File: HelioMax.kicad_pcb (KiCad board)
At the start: 2 copper layers, 185.3 x 159 mm, 75 parts, among them J2 Conn_01x07, J3 Conn_01x07, J4 Conn_01x07, J5 Conn_01x07, J8 Conn_01x07, J9 Conn_01x07, SW0:10 SW0:3, SW0:11 SW0:2, SW0:12 SW0:1, SW0:7 SW0:6, SW0:8 SW0:5, SW0:9 SW0:4, SW1:10 SW1:3, SW1:11 SW1:2, SW1:12 SW1:1, SW1:13 SW1:0, SW1:9 SW1:4, SW2:10 SW2:3, SW2:11 SW2:2, SW2:12 SW2:1, SW2:13 SW2:0, SW2:7 SW2:6, SW2:8 SW2:5, SW2:9 SW2:4, SW3:10 SW3:3, SW3:11 SW3:2, SW3:12 SW3:1, SW3:13 SW3:0, SW3:8 SW3:5, SW3:9 SW3:4, SW4:10 SW4:3, SW4:11 SW4:2, SW4:12 SW4:1, SW4:13 SW4:0, SW4:7 SW4:6, SW4:8 SW4:5, SW4:9 SW4:4, SW5:10 SW5:3, SW5:11 SW5:2, SW5:12 SW5:1, SW5:13 SW5:0, SW5:7 SW5:6, SW5:8 SW5:5, SW5:9 SW5:4, SW6:10 SW6:3, SW6:11 SW6:2, SW6:12 SW6:1, SW6:13 SW6:0, SW6:7 SW6:6, SW6:8 SW6:5, SW6:9 SW6:4

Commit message: Fixed edge cuts. Lots of DRC errors.
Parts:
- added ?: , , F.Cu at (85.2, 53.6)
- added ?: , , F.Cu at (40.5, 53.6)
- added ?: , , F.Cu at (40.5, 21.7)
- added A1: RaspberryPi_Pico, Module_RaspberryPi_Pico:RaspberryPi_Pico_Original_SMD_MountingHoles_HandSolder_Castellated, F.Cu at (63.1, 37.9)
- added J1: Conn_01x01_Pin, Connector_PinHeader_1.00mm:PinHeader_1x01_P1.00mm_Vertical, F.Cu at (48.1, 24.6)
- added J10: Conn_01x07, Connector_JST:JST_SH_SM08B-SRSS-TB_1x08-1MP_P1.00mm_Horizontal, F.Cu at (80.0, 20.9)
- added J11: Conn_01x07, Connector_JST:JST_SH_SM08B-SRSS-TB_1x08-1MP_P1.00mm_Horizontal, F.Cu at (64.5, 20.9)
- added J6: Conn_01x07, Connector_JST:JST_SH_SM08B-SRSS-TB_1x08-1MP_P1.00mm_Horizontal, F.Cu at (50.4, 54.7)
- added J7: Conn_01x07, Connector_JST:JST_SH_SM08B-SRSS-TB_1x08-1MP_P1.00mm_Horizontal, F.Cu at (71.6, 54.7)
- moved ? 70.4 mm to (209.5, 39.8)
- moved H99 70.4 mm to (121.1, 182.4)
- moved J3 70.4 mm to (150.5, 151.7)
- moved S1 70.4 mm to (119.7, 160.3)
- moved S2 70.4 mm to (138.8, 160.3)
- moved STITCHING_VIA 70.4 mm to (209.0, 74.1)
- moved STITCHING_VIA 70.4 mm to (152.4, 64.4)
- moved STITCHING_VIA 70.4 mm to (153.6, 77.0)
- moved STITCHING_VIA 70.4 mm to (190.6, 75.2)
- moved STITCHING_VIA 70.4 mm to (170.8, 134.0)
- moved STITCHING_VIA 70.4 mm to (94.5, 153.6)
- moved STITCHING_VIA 70.4 mm to (190.2, 138.6)
- moved STITCHING_VIA 70.4 mm to (208.9, 138.7)
- moved STITCHING_VIA 70.4 mm to (228.1, 137.1)
- moved SW0:10 70.4 mm to (138.8, 160.3)
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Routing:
- net Net-(A1-LED_OUT): track 0.00 -> 63.4 mm
- net Net-(A1-~{SMPS_PS}): track 0.00 -> 57.0 mm
- net Net-(A1-GPIO14): track 0.00 -> 38.4 mm
- net Net-(A1-GPIO15): track 0.00 -> 29.3 mm
- net Net-(J1-Pin_1): track 0.00 -> 20.3 mm
- net Net-(A1-GPIO0): track 0.00 -> 12.3 mm
- net Net-(A1-GPIO16): track 0.00 -> 11.9 mm
- net Net-(A1-GPIO1): track 0.00 -> 10.9 mm
- net Net-(A1-GPIO7): track 0.00 -> 10.9 mm
- net Net-(A1-GPIO6): track 0.00 -> 10.2 mm
- net Net-(A1-GPIO17): track 0.00 -> 10.1 mm
- net Net-(A1-GPIO8): track 0.00 -> 9.11 mm
- net Net-(A1-GPIO21): track 0.00 -> 9.11 mm
- net Net-(A1-GPIO13): track 0.00 -> 8.82 mm
- net Net-(A1-GPIO9): track 0.00 -> 7.90 mm
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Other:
- board size 185.3 x 159 mm -> 240.8 x 162.9 mm
- board text added: "Raspberry Pi Pico TP4 and TP5 must be modded to expose GP23 and GP25 respectively. J1 to be connected externally to GP24."
- board text added: "TP4"
- board text added: "TP5"

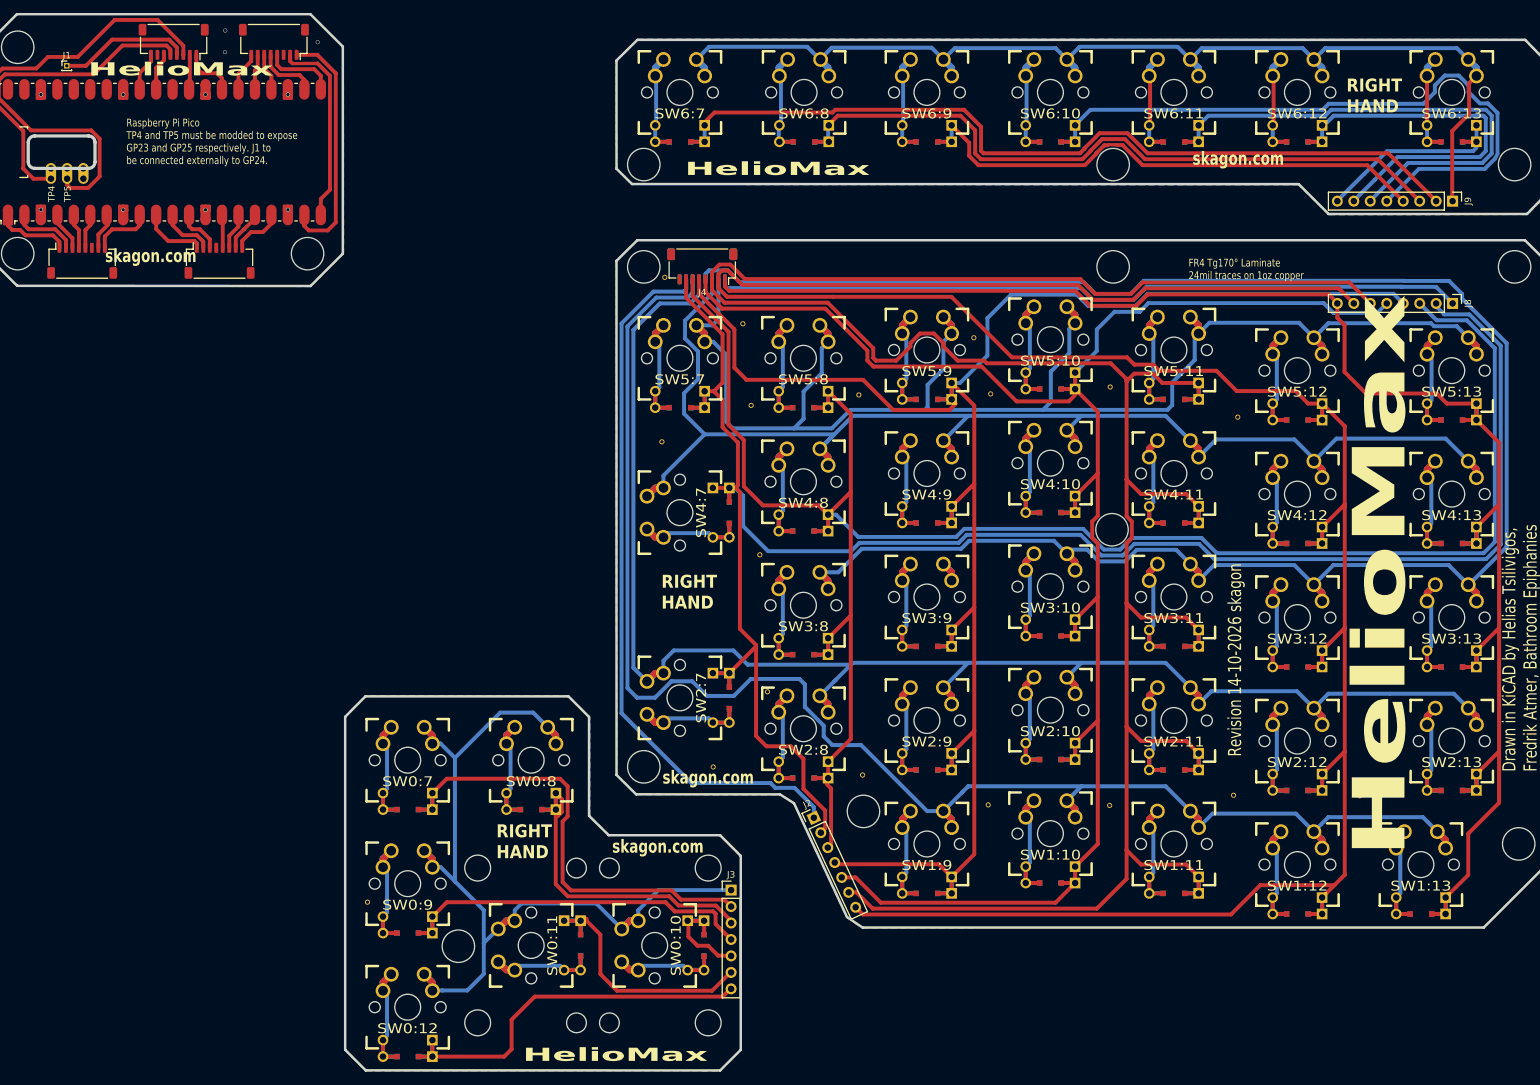
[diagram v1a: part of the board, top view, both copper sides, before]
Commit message: Updated switch footprint and fixed all wiring.
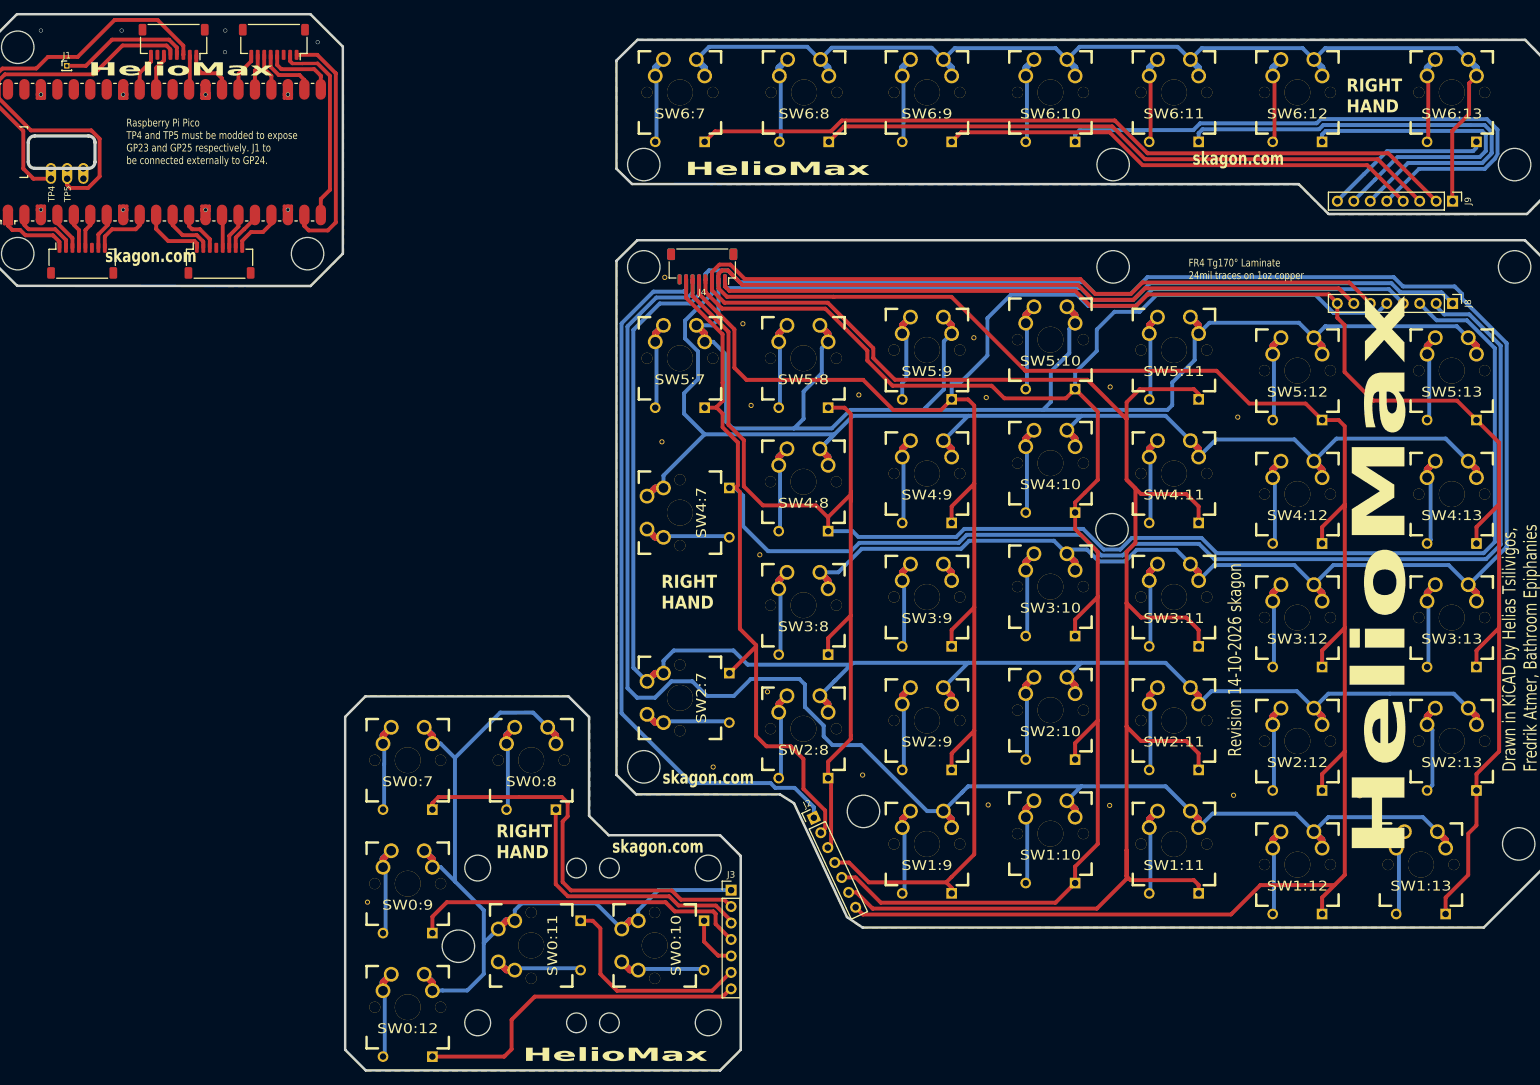
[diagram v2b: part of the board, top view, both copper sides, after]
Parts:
- SW0:10, SW0:11, SW0:12, SW0:7, SW0:8, SW0:9, SW1:10, SW1:11, SW1:12, SW1:13, SW1:9, SW2:10, SW2:11, SW2:12, SW2:13, SW2:7, SW2:8, SW2:9, SW3:10, SW3:11, SW3:12, SW3:13, SW3:8, SW3:9, SW4:10, SW4:11, SW4:12, SW4:13, SW4:7, SW4:8, SW4:9, SW5:10, SW5:11, SW5:12, SW5:13, SW5:7, SW5:8, SW5:9, SW6:10, SW6:11, SW6:12, SW6:13, SW6:7, SW6:8, SW6:9: footprint ErgoDOX pcb:MX_FLIP_DIODE -> ErgoDOX pcb:MX_FLIP_CLEAN
- moved STITCHING_VIA 0.89 mm to (189.9, 75.8)
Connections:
- J10 pad MP: GND -> (no net)
- J11 pad MP: GND -> (no net)
- J6 pad MP: GND -> (no net)
- J7 pad MP: GND -> (no net)
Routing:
- net /COL3: track 393.8 -> 361.6 mm
- net /COL6: track 491.5 -> 461.9 mm
- net /COL5: track 455.4 -> 429.4 mm
- net /COL1: track 514.9 -> 490.3 mm
- net /COL2: track 507.9 -> 483.3 mm
- net /COL0: track 275.2 -> 251.9 mm
- net /COL4: track 407.6 -> 386.4 mm
- net Net-(SW2:7-A): track 19.4 -> 16.4 mm
- net Net-(SW4:7-A): track 19.4 -> 16.4 mm
- net Net-(SW0:10-A): track 19.4 -> 16.4 mm
- net Net-(SW2:12-A): track 19.4 -> 16.4 mm
- net Net-(SW5:7-A): track 19.4 -> 16.4 mm
- net Net-(SW5:12-A): track 19.4 -> 16.4 mm
- net Net-(SW3:12-A): track 19.4 -> 16.4 mm
- net Net-(SW1:12-A): track 19.4 -> 16.4 mm
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
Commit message: Fixed most DRC problems, new vias, modified switch footprints.
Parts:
- removed STITCHING_VIA (x18): ~, lib_footprints:STITCHING_VIA
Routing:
- net /ROW3: track 317.5 -> 320.8 mm
- net /COL2: track 483.3 -> 486.3 mm
- net /COL5: track 429.4 -> 428.1 mm
- net /ROW1: track 249.8 -> 248.7 mm
- net /COL3: track 361.6 -> 362.6 mm
- net /ROW2: track 260.8 -> 260.0 mm
- net GND: vias 13 -> 47

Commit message: Replace relic holes, include fonts, general clean-up and rewiring.
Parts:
- removed ? (x6): , 
- removed H99: MECHANICAL, ErgoDOXmech
- added H1: MountingHole, MountingHole:MountingHole_3.2mm_M3, F.Cu at (134.6, 60.2)
- added H10: MountingHole, MountingHole:MountingHole_3.2mm_M3, F.Cu at (206.2, 44.2)
- added H11: MountingHole, MountingHole:MountingHole_3.2mm_M3, F.Cu at (268.1, 44.2)
- added H12: MountingHole, MountingHole:MountingHole_3.2mm_M3, F.Cu at (29.6, 29.2)
- added H13: MountingHole, MountingHole:MountingHole_3.2mm_M3, F.Cu at (29.6, 61.0)
- added H14: MountingHole, MountingHole:MountingHole_3.2mm_M3, F.Cu at (74.3, 61.0)
- added H2: MountingHole, MountingHole:MountingHole_3.2mm_M3, F.Cu at (207.0, 60.2)
- added H3: MountingHole, MountingHole:MountingHole_3.2mm_M3, F.Cu at (269.0, 60.2)
- added H4: MountingHole, MountingHole:MountingHole_3.2mm_M3, F.Cu at (134.6, 137.3)
- added H5: MountingHole, MountingHole:MountingHole_3.2mm_M3, F.Cu at (206.9, 100.7)
- added H6: MountingHole, MountingHole:MountingHole_3.2mm_M3, F.Cu at (269.6, 149.2)
- added H7: MountingHole, MountingHole:MountingHole_3.2mm_M3, F.Cu at (168.9, 150.0)
- added H8: MountingHole, MountingHole:MountingHole_3.2mm_M3, F.Cu at (100.9, 167.8)
- added H9: MountingHole, MountingHole:MountingHole_3.2mm_M3, F.Cu at (133.8, 44.2)
- moved A1 13.3 mm to (52.2, 45.4)
- moved J6 13.3 mm to (39.5, 62.1)
- moved J7 13.3 mm to (60.7, 62.1)
- moved J10 13.3 mm to (69.1, 28.4)
- moved J11 13.3 mm to (53.6, 28.4)
- moved J3 10.6 mm to (143.0, 159.1)
- moved S2 10.6 mm to (131.2, 167.7)
- moved SW0:10 10.6 mm to (131.2, 167.7)
- moved SW0:12 10.6 mm to (93.1, 177.2)
- moved SW0:7 10.6 mm to (93.1, 139.1)
- moved S1 10.6 mm to (112.1, 167.7)
- moved SW0:11 10.6 mm to (112.1, 167.7)
- moved SW0:8 10.6 mm to (112.1, 139.1)
- moved SW0:9 10.6 mm to (93.1, 158.1)
- moved J9 5.49 mm to (258.5, 49.8)
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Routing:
- net /COL2: track 486.3 -> 456.3 mm
- net Net-(J1-Pin_1): track 20.3 -> 11.6 mm
- net /COL4: track 386.4 -> 383.5 mm
- net GND: vias 47 -> 46
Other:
- board size 240.8 x 162.9 mm -> 249.3 x 162.8 mm
- board text added: "Rev 1 — 17-10-2026 skagon"
- board text removed: "Revision 14-10-2026 skagon"
